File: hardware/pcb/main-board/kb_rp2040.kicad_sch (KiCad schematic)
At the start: 28 parts, among them J1201 Conn_01x02, J1202 Conn_01x02, U1202 W25Q32JVSNIQ, U1203 RP2040, Y1201 ABLS-12.000MHZ-B4-T

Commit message: tidy the keyboard comms
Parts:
- removed J1202: Conn_01x02, symbol Connector_Generic:Conn_01x02
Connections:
- net KB_TX_TO_APPB1: now reaches U1203.29 (GPIO18)
- net KB_RX_FROM_APPB1: now reaches U1203.30 (GPIO19)
- net RX_FROM_SP_RP renamed KB_RX_FROM_APPB0
- net TX_TO_SP_RP renamed KB_TX_TO_APPB0
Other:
- note added: "Software connection to the application board's Pico1. (No UART available for this.)"
- note added: "UART connection to the application board's Pico0"
- note removed: "These can be used to send keypresses to other parts of the system. Probably only need one signal, not the pair"
- note removed: "UART connection to the support RP2040. That device will need to receive keypresses and forward them to the application board."
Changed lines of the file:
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@@
 	)
 	(no_connect
-		(at 120.65 130.81)
+		(at 120.65 128.27)
 	)
 	(no_connect
-		(at 120.65 146.05)
+		(at 120.65 130.81)
 	)
 	(no_connect
-		(at 120.65 123.19)
+		(at 120.65 146.05)
 	)
 	(no_connect
@@
 	(wire
 		(pts
-			(xy 105.41 125.73) (xy 123.19 125.73)
+			(xy 105.41 125.73) (xy 120.65 125.73)
 		)
 		(stroke
@@
 	(wire
 		(pts
-			(xy 105.41 128.27) (xy 123.19 128.27)
+			(xy 105.41 128.27) (xy 120.65 128.27)
 		)
 		(stroke
@@
 		)
 	)
+	(text "Software connection to the application board's Pico1.\n(No UART available for this.)"
+		(exclude_from_sim no)
+		(at 144.78 124.46 0)
+		(effects
+			(font
+				(size 1 1)
+			)
+			(justify left)
+		)
+	)
 	(text "Enabled by RP2040. Don't bother with the\nBOOTSEL switch unless there's a problem."
 		(exclude_from_sim no)
@@
 		)
 	)
-	(text "UART connection to the support RP2040.\nThat device will need to receive\nkeypresses and forward them to the\napplication board."
+	(text "UART connection to the application board's Pico0"
 		(exclude_from_sim no)
 		(at 144.78 119.38 0)
@@
 		)
 	)
-	(text "These can be used to send keypresses\nto other parts of the system. Probably\nonly need one signal, not the pair"
-		(exclude_from_sim no)
-		(at 144.78 127 0)
-		(effects
-			(font
-				(size 1 1)
-			)
-			(justify left)
-		)
-	)
 	(label "XOUT"
 		(at 275.59 100.33 180)
@@
 		)
 	)
-	(global_label "TX_TO_SP_RP"
+	(global_label "KB_TX_TO_APPB0"
 		(shape output)
 		(at 120.65 118.11 0)
@@
 		)
 		(property "Intersheetrefs" "${INTERSHEET_REFS}"
-			(at 135.3785 118.11 0)
+			(at 139.0071 118.11 0)
 			(effects
 				(font
@@
 		)
 	)
+	(global_label "KB_TX_TO_APPB1"
+		(shape output)
+		(at 120.65 123.19 0)
+		(fields_autoplaced yes)
+		(effects
+			(font
+				(size 1.27 1.27)
+			)
+			(justify left)
+		)
+		(property "Intersheetrefs" "${INTERSHEET_REFS}"
+			(at 139.0071 123.19 0)
+			(effects
+				(font
+					(size 1.27 1.27)
+				)
+				(justify left)
+				(hide yes)
+			)
+		)
+	)
 	(global_label "KB_A10"
 		(shape output)
@@
 		)
 	)
-	(global_label "RX_FROM_SP_RP"
+	(global_label "KB_RX_FROM_APPB0"
 		(shape input)
 		(at 120.65 120.65 0)
@@
 		)
 		(property "Intersheetrefs" "${INTERSHEET_REFS}"
-			(at 138.5233 120.65 0)
+			(at 142.1519 120.65 0)
+			(effects
+				(font
+					(size 1.27 1.27)
+				)
+				(justify left)
+				(hide yes)
+			)
+		)
+	)
+	(global_label "KB_RX_FROM_APPB1"
+		(shape input)
+		(at 120.65 125.73 0)
+		(fields_autoplaced yes)
+		(effects
+			(font
+				(size 1.27 1.27)
+			)
+			(justify left)
+		)
+		(property "Intersheetrefs" "${INTERSHEET_REFS}"
+			(at 142.1519 125.73 0)
 			(effects
 				(font
@@
 					(unit 1)
 				)
-			)
-		)
-	)
-	(symbol
-		(lib_id "Connector_Generic:Conn_01x02")
-		(at 128.27 125.73 0)
-		(unit 1)
-		(exclude_from_sim no)
-		(in_bom yes)
-		(on_board yes)
-		(dnp no)
-		(fields_autoplaced yes)
-		(property "Reference" "J1202"
-			(at 130.81 125.7299 0)
-			(effects
-				(font
-					(size 1.27 1.27)
-				)
-				(justify left)
-			)
-		)
-		(property "Value" "Conn_01x02"
-			(at 130.81 128.2699 0)
-			(effects
-				(font
-					(size 1.27 1.27)
-				)
-				(justify left)
-			)
-		)
-		(property "Footprint" ""
-			(at 128.27 125.73 0)
-			(effects
-				(font
-					(size 1.27 1.27)
-				)
-				(hide yes)
-			)
-		)
-		(property "Datasheet" "~"
-			(at 128.27 125.73 0)
-			(effects
-				(font
-					(size 1.27 1.27)
-				)
-				(hide yes)
-			)
-		)
-		(property "Description" "Generic connector, single row, 01x02, script generated (kicad-library-utils/schlib/autogen/connector/)"
-			(at 128.27 125.73 0)
-			(effects
-				(font
-					(size 1.27 1.27)
-				)
-				(hide yes)
-			)
-		)
-		(pin "2"
-		)
-		(pin "1"
-		)
-		(instances
-			(project ""
-				(path "/fdce8012-5f35-4f58-8abb-80214b4af8fe/bd010eea-67e1-4f0f-9c21-5375d46a1c97"
-					(reference "J1202")
-					(unit 1)
-				)

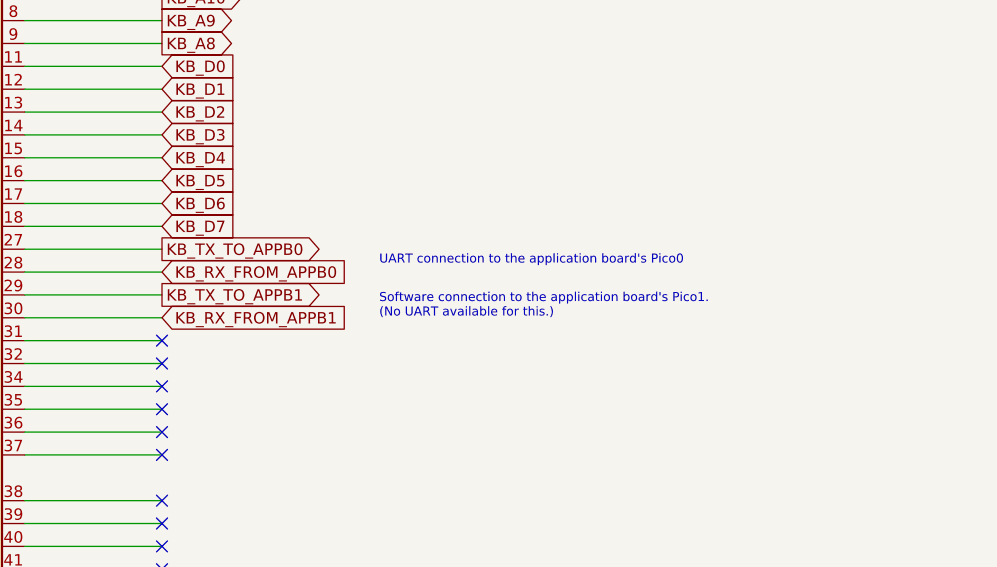
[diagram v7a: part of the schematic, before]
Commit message: rename app board picos to 1 and 2, to match the application board schematics
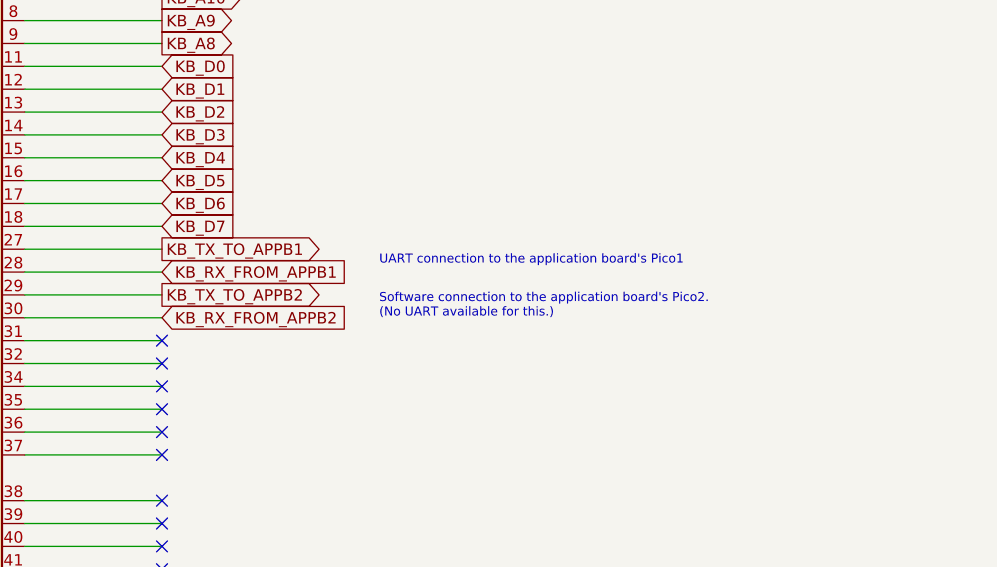
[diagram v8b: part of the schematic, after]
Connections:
- net KB_RX_FROM_APPB0 is gone; now on net KB_RX_FROM_APPB1: U1203.28 (GPIO17)
- net KB_TX_TO_APPB0 is gone; now on net KB_TX_TO_APPB1: U1203.27 (GPIO16)
- net KB_RX_FROM_APPB1: no longer U1203.30 (GPIO19)
- net KB_TX_TO_APPB1: no longer U1203.29 (GPIO18)
- new net KB_RX_FROM_APPB2: U1203.30 (GPIO19)
- new net KB_TX_TO_APPB2: U1203.29 (GPIO18)
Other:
- note added: "Software connection to the application board's Pico2. (No UART available for this.)"
- note added: "UART connection to the application board's Pico1"
- note removed: "Software connection to the application board's Pico1. (No UART available for this.)"
- note removed: "UART connection to the application board's Pico0"
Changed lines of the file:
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@@
 		)
 	)
-	(text "Software connection to the application board's Pico1.\n(No UART available for this.)"
+	(text "Software connection to the application board's Pico2.\n(No UART available for this.)"
 		(exclude_from_sim no)
 		(at 144.78 124.46 0)
@@
 		)
 	)
-	(text "UART connection to the application board's Pico0"
+	(text "UART connection to the application board's Pico1"
 		(exclude_from_sim no)
 		(at 144.78 119.38 0)
@@
 		)
 	)
-	(global_label "KB_TX_TO_APPB0"
+	(global_label "KB_TX_TO_APPB1"
 		(shape output)
 		(at 120.65 118.11 0)
@@
 		)
 	)
-	(global_label "KB_TX_TO_APPB1"
+	(global_label "KB_TX_TO_APPB2"
 		(shape output)
 		(at 120.65 123.19 0)
@@
 		)
 	)
-	(global_label "KB_RX_FROM_APPB0"
+	(global_label "KB_RX_FROM_APPB1"
 		(shape input)
 		(at 120.65 120.65 0)
@@
 		)
 	)
-	(global_label "KB_RX_FROM_APPB1"
+	(global_label "KB_RX_FROM_APPB2"
 		(shape input)
 		(at 120.65 125.73 0)
